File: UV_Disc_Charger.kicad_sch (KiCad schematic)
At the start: 40 parts, among them J2 JST PH Connector, J2 Type-C_6P, J3 Conn_01x01, J4 JST PH Connector, J5 JST PH Connector, J6 JST PH Connector, J7 Conn_01x01, U1 TP4056, U2 DW01A, U3 FS8205A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

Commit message: layout started
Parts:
- removed R1: 2512 package, Resistor_SMD:R_2512_6332Metric, symbol Device:R
- removed R2: 0R2 to 0R5, Resistor_SMD:R_0805_2012Metric, symbol Device:R
- added D4: SS34, Diode_SMD:D_SMA, symbol Device:D_Schottky
- added F1: 1.5A, Fuse:Fuse_1206_3216Metric, symbol Device:Fuse
- added Q1, Q2: SI2301, Package_TO_SOT_SMD:SOT-23, symbol Device:Q_PMOS_GSD
- added R13: 1k, Resistor_SMD:R_0805_2012Metric, symbol Device:R
- added R14: 10k, Resistor_SMD:R_0805_2012Metric, symbol Device:R
- added R15: 0R4, Resistor_SMD:R_0805_2012Metric, symbol Device:R
- added R16: 2512 package, Resistor_SMD:R_2512_6332Metric, symbol Device:R
- added SW1: SW_SPST, Connector_PinHeader_2.54mm:PinHeader_1x02_P2.54mm_Vertical, symbol Switch:SW_SPST
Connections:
- net +BATT: now also SW1.2 (B); no longer C1.1, C4.1, C5.1, R3.2, U1.5 (BAT), U4.10 (VIN), U4.11 (VIN)
- net GND: now also R14.2
- net VBUS: now also D4.2 (A), R13.2, R14.1, R15.2, R16.2
- net at C2.1, D2.2 (A), D3.2 (A)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: now also R15.1, R16.1
- new net: Q1.1 (G), Q2.1 (G), R13.1
- new net: C1.1, F1.2, Q1.2 (S), R3.2, U1.5 (BAT)
- new net: Q1.3 (D), Q2.3 (D)
- new net: F1.1, SW1.1 (A)
- new net VCC: C4.1, C5.1, D4.1 (K), Q2.2 (S), U4.10 (VIN), U4.11 (VIN)
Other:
- added sheet LEDS (LEDS.kicad_sch)
- note added: "UV LEDS"
- moved on the sheet: C1, C2, C3, D2, D3, J6, R3, R4, R5, R8, R9, U1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

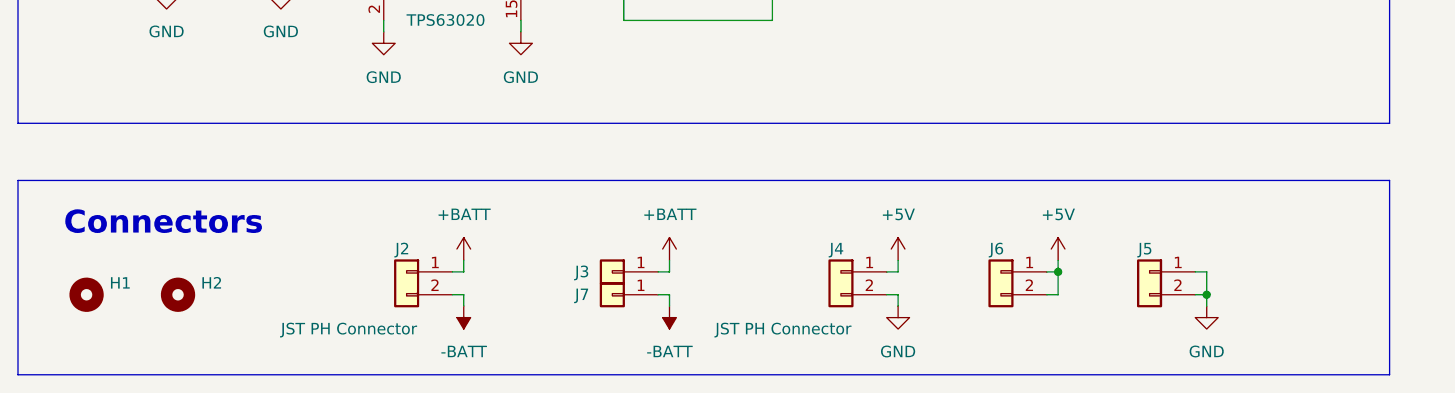
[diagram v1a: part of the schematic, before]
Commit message: added manufacturing files
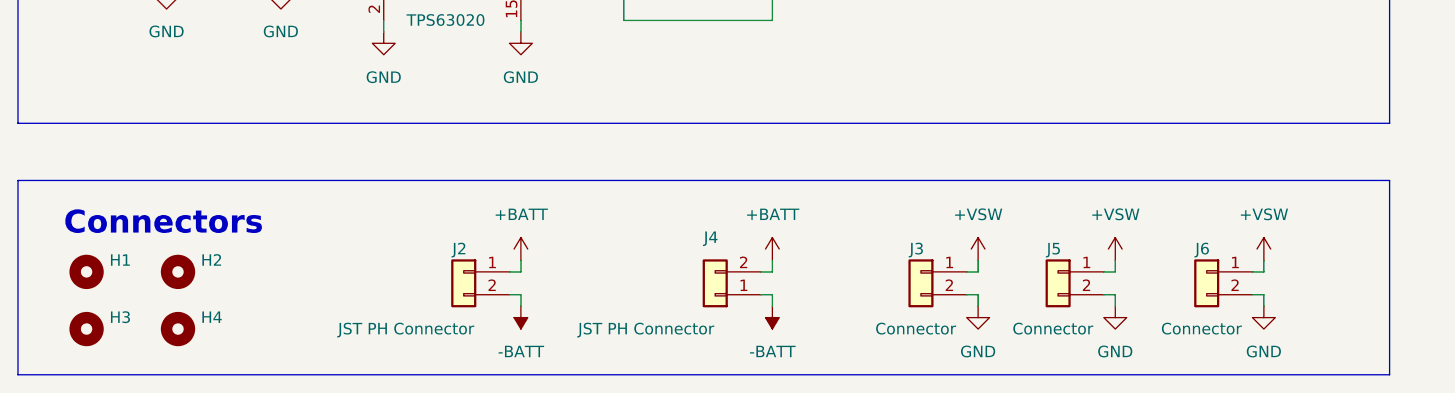
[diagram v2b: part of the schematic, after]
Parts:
- removed J3, J7: Conn_01x01, Connector_PinHeader_2.54mm:PinHeader_1x01_P2.54mm_Vertical, symbol Connector_Generic:Conn_01x01
- added H3, H4: MountingHole, MountingHole:MountingHole_3.2mm_M3_DIN965_Pad, symbol Mechanical:MountingHole
- added J3: Connector, Connector_PinHeader_2.54mm:PinHeader_1x02_P2.54mm_Vertical, symbol Connector_Generic:Conn_01x02
- J4: footprint Connector_JST:JST_PH_B2B-PH-K_1x02_P2.00mm_Vertical -> Connector_JST:JST_PH_S2B-PH-SM4-TB_1x02-1MP_P2.00mm_Horizontal
- J5, J6: value JST PH Connector -> Connector
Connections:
- net +5V: no longer J4.1 (Pin_1), J6.1 (Pin_1), J6.2 (Pin_2)
- net +BATT: now also J4.2 (Pin_2)
- net -BATT: now also J4.1 (Pin_1)
- net GND: now also J6.2 (Pin_2), J3.2 (Pin_2); no longer J4.2 (Pin_2), J5.1 (Pin_1)
- new net +VSW: J3.1 (Pin_1), J5.1 (Pin_1), J6.1 (Pin_1)
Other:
- moved on the sheet: H1, H2, J2
